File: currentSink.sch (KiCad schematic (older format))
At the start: 6 parts, among them P101 ExtBatt_Power, P102 uPower, P103 uSignals, P104 Load+ve, P105 Load-ve, SW101 SWITCH_INV

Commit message: updated project with most footprint associations
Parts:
- removed SW101: SWITCH_INV, symbol SWITCH_INV
- added P106: PowerSwitch, Pin_Headers:Pin_Header_Straight_1x03, symbol CONN_01X03
- P102: footprint (none) -> Pin_Headers:Pin_Header_Straight_1x02
- P103: footprint (none) -> Pin_Headers:Pin_Header_Straight_1x05
- P104, P105: footprint (none) -> Pin_Headers:Pin_Header_Straight_1x01
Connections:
- wire segments 51 -> 52
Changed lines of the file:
@@
 F 0 "P105" H 9650 3800 50  0000 C CNN
 F 1 "Load-ve" V 9750 3700 50  0000 C CNN
-F 2 "" H 9650 3700 60  0000 C CNN
+F 2 "Pin_Headers:Pin_Header_Straight_1x01" H 9650 3700 60  0001 C CNN
 F 3 "" H 9650 3700 60  0000 C CNN
 	1    9650 3700
@@
 F 0 "P104" H 9650 1150 50  0000 C CNN
 F 1 "Load+ve" V 9750 1050 50  0000 C CNN
-F 2 "" H 9650 1050 60  0000 C CNN
+F 2 "Pin_Headers:Pin_Header_Straight_1x01" H 9650 1050 60  0001 C CNN
 F 3 "" H 9650 1050 60  0000 C CNN
 	1    9650 1050
@@
 F 0 "P103" H 1300 5600 50  0000 C CNN
 F 1 "uSignals" V 1400 5300 50  0000 C CNN
-F 2 "" H 1300 5300 60  0000 C CNN
+F 2 "Pin_Headers:Pin_Header_Straight_1x05" H 1300 5300 60  0001 C CNN
 F 3 "" H 1300 5300 60  0000 C CNN
 	1    1300 5300
@@
 $EndComp
 $Comp
-L GND #PWR01
+L GND #PWR103
 U 1 1 552165DD
 P 9450 4050
-F 0 "#PWR01" H 9450 3800 60  0001 C CNN
+F 0 "#PWR103" H 9450 3800 60  0001 C CNN
 F 1 "GND" H 9450 3900 60  0000 C CNN
 F 2 "" H 9450 4050 60  0000 C CNN
@@
 F 0 "P102" H 1300 3250 50  0000 C CNN
 F 1 "uPower" V 1400 3100 50  0000 C CNN
-F 2 "" H 1300 3100 60  0000 C CNN
+F 2 "Pin_Headers:Pin_Header_Straight_1x02" H 1300 3100 60  0001 C CNN
 F 3 "" H 1300 3100 60  0000 C CNN
 F 4 "Value" H 1300 3100 60  0001 C CNN "MPN"
@@
 $EndComp
 $Comp
-L GND #PWR02
+L GND #PWR102
 U 1 1 55229C45
 P 1900 2700
-F 0 "#PWR02" H 1900 2450 60  0001 C CNN
+F 0 "#PWR102" H 1900 2450 60  0001 C CNN
 F 1 "GND" H 1900 2550 60  0000 C CNN
 F 2 "" H 1900 2700 60  0000 C CNN
@@
 Wire Wire Line
 	4800 4350 4800 3200
-$Comp
-L SWITCH_INV SW101
-U 1 1 5521E775
-P 4400 1450
-F 0 "SW101" H 4200 1600 50  0000 C CNN
-F 1 "SWITCH_INV" H 4250 1300 50  0000 C CNN
-F 2 "" H 4400 1450 60  0000 C CNN
-F 3 "" H 4400 1450 60  0000 C CNN
-	1    4400 1450
-	0    1    -1   0
-$EndComp
-Wire Wire Line
-	4500 950  4500 700
-Wire Wire Line
-	4500 700  7500 700
 Connection ~ 7500 1400
 Wire Wire Line
-	4400 1950 5150 1950
+	3950 1950 5150 1950
 Wire Wire Line
 	5150 1950 5150 1700
@@
 F 0 "P101" H 1300 1550 50  0000 C CNN
 F 1 "ExtBatt_Power" V 1400 1400 50  0000 C CNN
-F 2 "" H 1300 1400 60  0000 C CNN
+F 2 "" H 1300 1400 60  0001 C CNN
 F 3 "" H 1300 1400 60  0000 C CNN
 	1    1300 1400
@@
 $EndComp
 Wire Wire Line
-	1450 1450 3350 1450
-Wire Wire Line
-	3350 1450 3350 700
-Wire Wire Line
-	3350 700  4300 700
-Wire Wire Line
-	4300 700  4300 950
-$Comp
-L GND #PWR03
+	1450 1450 3850 1450
+$Comp
+L GND #PWR101
 U 1 1 5521EED5
 P 1900 950
-F 0 "#PWR03" H 1900 700 60  0001 C CNN
+F 0 "#PWR101" H 1900 700 60  0001 C CNN
 F 1 "GND" H 1900 800 60  0000 C CNN
 F 2 "" H 1900 950 60  0000 C CNN
@@
 Wire Wire Line
 	1900 750  1900 950
+Wire Wire Line
+	4500 700  7500 700
+$Comp
+L CONN_01X03 P106
+U 1 1 5528D1C9
+P 3950 750
+F 0 "P106" H 3950 950 50  0000 C CNN
+F 1 "PowerSwitch" V 4050 750 50  0000 C CNN
+F 2 "Pin_Headers:Pin_Header_Straight_1x03" H 3950 750 60  0001 C CNN
+F 3 "" H 3950 750 60  0000 C CNN
+	1    3950 750
+	0    -1   -1   0
+$EndComp
+Wire Wire Line
+	3850 1450 3850 950
+Wire Wire Line
+	4500 700  4500 1450
+Wire Wire Line
+	4500 1450 4050 1450
+Wire Wire Line
+	4050 1450 4050 950
+Wire Wire Line
+	3950 1950 3950 950
 $EndSCHEMATC

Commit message: association of footprints complete
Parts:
- P101: footprint (none) -> Pin_Headers:Pin_Header_Straight_1x02
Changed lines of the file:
@@
 $EndComp
 $Comp
-L GND #PWR103
+L GND #PWR01
 U 1 1 552165DD
 P 9450 4050
-F 0 "#PWR103" H 9450 3800 60  0001 C CNN
+F 0 "#PWR01" H 9450 3800 60  0001 C CNN
 F 1 "GND" H 9450 3900 60  0000 C CNN
 F 2 "" H 9450 4050 60  0000 C CNN
@@
 $EndComp
 $Comp
-L GND #PWR102
+L GND #PWR02
 U 1 1 55229C45
 P 1900 2700
-F 0 "#PWR102" H 1900 2450 60  0001 C CNN
+F 0 "#PWR02" H 1900 2450 60  0001 C CNN
 F 1 "GND" H 1900 2550 60  0000 C CNN
 F 2 "" H 1900 2700 60  0000 C CNN
@@
 F 0 "P101" H 1300 1550 50  0000 C CNN
 F 1 "ExtBatt_Power" V 1400 1400 50  0000 C CNN
-F 2 "" H 1300 1400 60  0001 C CNN
+F 2 "Pin_Headers:Pin_Header_Straight_1x02" H 1300 1400 60  0001 C CNN
 F 3 "" H 1300 1400 60  0000 C CNN
 	1    1300 1400
@@
 	1450 1450 3850 1450
 $Comp
-L GND #PWR101
+L GND #PWR03
 U 1 1 5521EED5
 P 1900 950
-F 0 "#PWR101" H 1900 700 60  0001 C CNN
+F 0 "#PWR03" H 1900 700 60  0001 C CNN
 F 1 "GND" H 1900 800 60  0000 C CNN
 F 2 "" H 1900 950 60  0000 C CNN

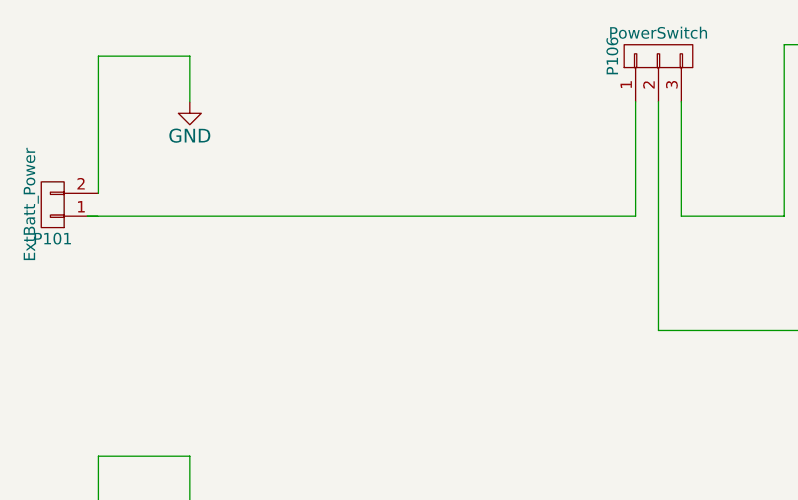
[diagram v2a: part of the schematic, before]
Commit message: removed duplicates and bad wire connections to enable the generation of a PCB
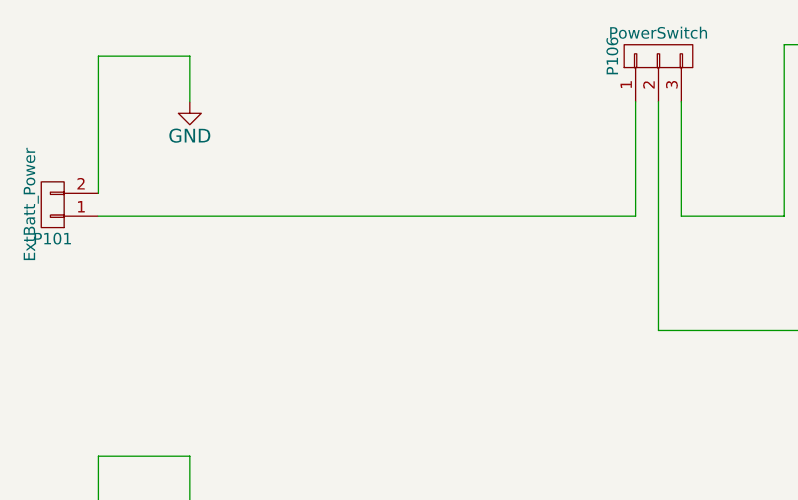
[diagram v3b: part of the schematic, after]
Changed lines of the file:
@@
 	-1   0    0    1
 $EndComp
-Wire Wire Line
-	1450 1450 3850 1450
 $Comp
 L GND #PWR03
@@
 Wire Wire Line
 	3950 1950 3950 950
+Wire Wire Line
+	1500 1450 3850 1450
 $EndSCHEMATC

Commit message: initial layout complete with gnd plane
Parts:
- P104, P105: footprint Pin_Headers:Pin_Header_Straight_1x01 -> Connect:1pin
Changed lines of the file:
@@
 F 0 "P105" H 9650 3800 50  0000 C CNN
 F 1 "Load-ve" V 9750 3700 50  0000 C CNN
-F 2 "Pin_Headers:Pin_Header_Straight_1x01" H 9650 3700 60  0001 C CNN
+F 2 "Connect:1pin" H 9650 3700 60  0001 C CNN
 F 3 "" H 9650 3700 60  0000 C CNN
 	1    9650 3700
@@
 F 0 "P104" H 9650 1150 50  0000 C CNN
 F 1 "Load+ve" V 9750 1050 50  0000 C CNN
-F 2 "Pin_Headers:Pin_Header_Straight_1x01" H 9650 1050 60  0001 C CNN
+F 2 "Connect:1pin" H 9650 1050 60  0001 C CNN
 F 3 "" H 9650 1050 60  0000 C CNN
 	1    9650 1050

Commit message: updated schematic with part numbers to ICs
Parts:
- P104: MPN (none) -> BU-P2143-0
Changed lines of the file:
@@
 F 1 "Load+ve" V 9750 1050 50  0000 C CNN
 F 2 "Connect:1pin" H 9650 1050 60  0001 C CNN
-F 3 "" H 9650 1050 60  0000 C CNN
+F 3 "http://muellerelectric.com/wp-content/uploads/BU-P2143-0.pdf" H 9650 1050 60  0001 C CNN
+F 4 "BU-P2143-0" H 9650 1050 60  0001 C CNN "MPN"
 	1    9650 1050
 	1    0    0    -1
